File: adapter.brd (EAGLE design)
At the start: 88.6 x 82.5 mm, 11 parts

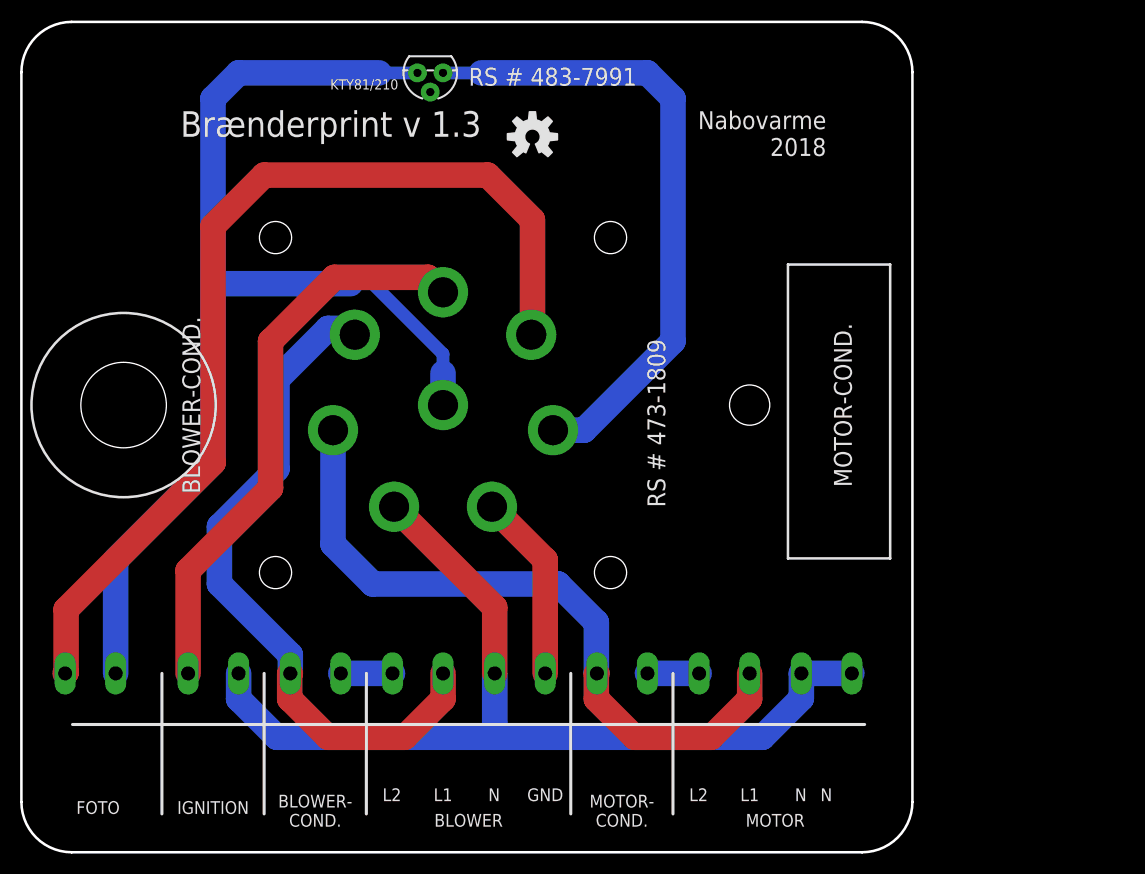
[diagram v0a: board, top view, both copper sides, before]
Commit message: new version (v.1.4)
socket pin spacing changed from 5,02 mm to 5 mm

grouped photo and ignition connectors

added more silk info

wider pcb with space for capacitor hole mount
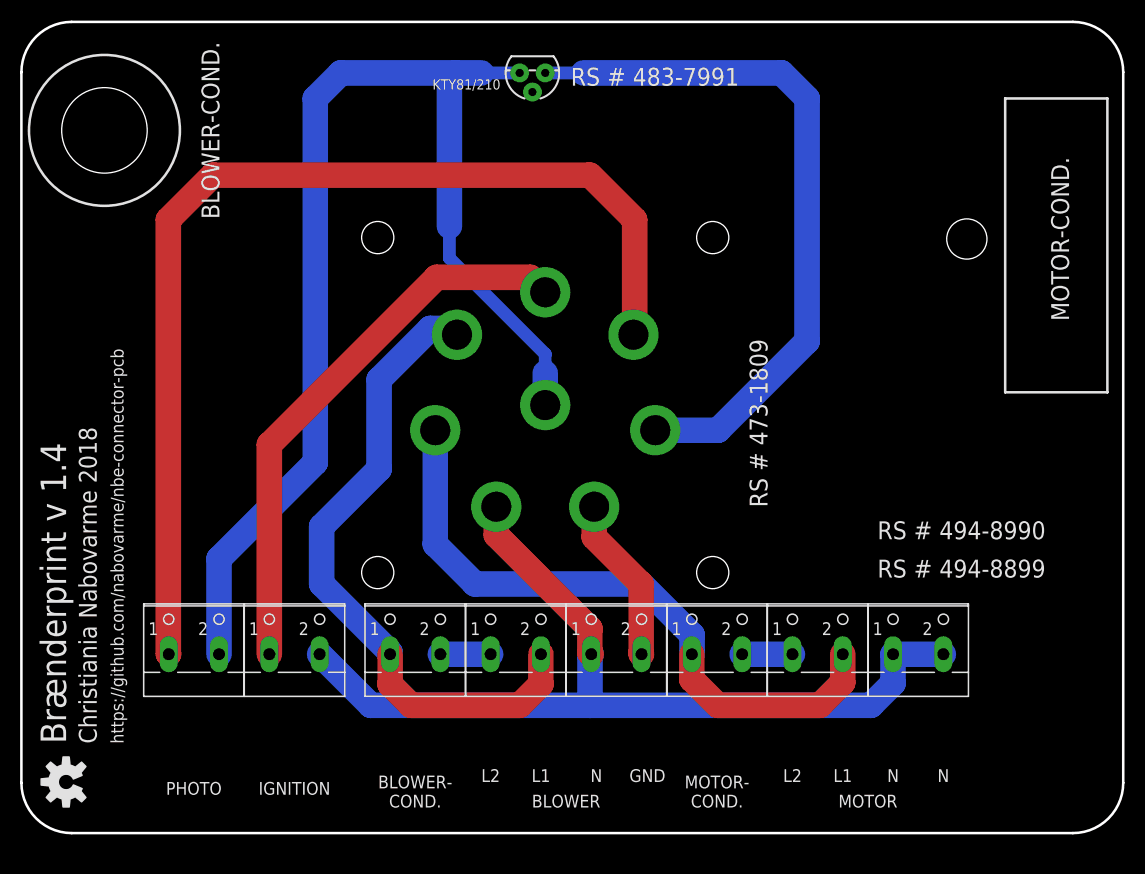
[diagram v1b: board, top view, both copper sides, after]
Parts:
- removed BLOWER1, FOTO, MOTOR1: (no value), SparkFun (old):1X02_LONGPADS
- added BLOWER-2, MOTOR-2, PHOTO: (no value), con-wago-500:W237-102
- BLOWER, BLOWER-COND., IGNITION, MOTOR, MOTOR-COND.: device SparkFun (old):1X02_LONGPADS -> con-wago-500:W237-102
- moved U$2 79.1 mm to (5.71, 4.45), turned to 90 degrees
- moved KTY81/210 10.2 mm to (52.1, 74.9)
- moved U$1 10.2 mm to (53.3, 41.9)
- moved BLOWER-COND. 8.05 mm to (40.4, 18.4), turned to 0 degrees
- moved BLOWER 7.90 mm to (50.4, 18.4), turned to 0 degrees
- moved MOTOR-COND. 7.61 mm to (70.4, 18.4), turned to 0 degrees
- moved MOTOR 7.46 mm to (80.4, 18.4), turned to 0 degrees
- moved IGNITION 6.40 mm to (28.4, 18.4), turned to 0 degrees
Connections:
- net GND: now also BLOWER-2.1, IGNITION.2, MOTOR-2.1, MOTOR-2.2; no longer BLOWER1.2, IGNITION.1, MOTOR1.1, MOTOR1.2
- net N$1: now also PHOTO.1; no longer FOTO.1
- net N$10: now also MOTOR-COND..1, MOTOR.2; no longer MOTOR-COND..2, MOTOR.1
- net N$2: now also IGNITION.1; no longer IGNITION.2
- net N$3: now also PHOTO.2; no longer FOTO.2
- net N$5: now also MOTOR-COND..2, MOTOR.1; no longer MOTOR-COND..1, MOTOR.2
- net N$7: now also BLOWER-COND..1, BLOWER.2; no longer BLOWER-COND..2, BLOWER.1
- net N$8: now also BLOWER-2.2; no longer BLOWER1.1
- net N$9: now also BLOWER-COND..2, BLOWER.1; no longer BLOWER-COND..1, BLOWER.2
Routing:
- net N$1: track 97.7 -> 104.7 mm
- net N$4: track 63.6 -> 70.0 mm
- net GND: track 96.2 -> 91.6 mm
- net N$10: track 69.3 -> 64.9 mm
- net N$3: track 113.4 -> 117.8 mm
- net N$7: track 68.1 -> 65.3 mm
- net N$8: track 18.8 -> 16.6 mm
- net N$2: track 56.8 -> 55.8 mm
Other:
- board size 88.6 x 82.5 mm -> 109.5 x 80.6 mm
- board text added: "Brænderprint v 1.4"
- board text added: "Christiania Nabovarme 2018"
- board text added: "PHOTO"
- board text added: "RS # 494-8899"
- board text added: "RS # 494-8990"
- board text added: "https://github.com/nabovarme/nbe-connector-pcb"
- board text removed: "Brænderprint v 1.3"
- board text removed: "FOTO"
- board text removed: "Nabovarme 2018"

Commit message: center aligned main connector on pcb
version 1.4.1
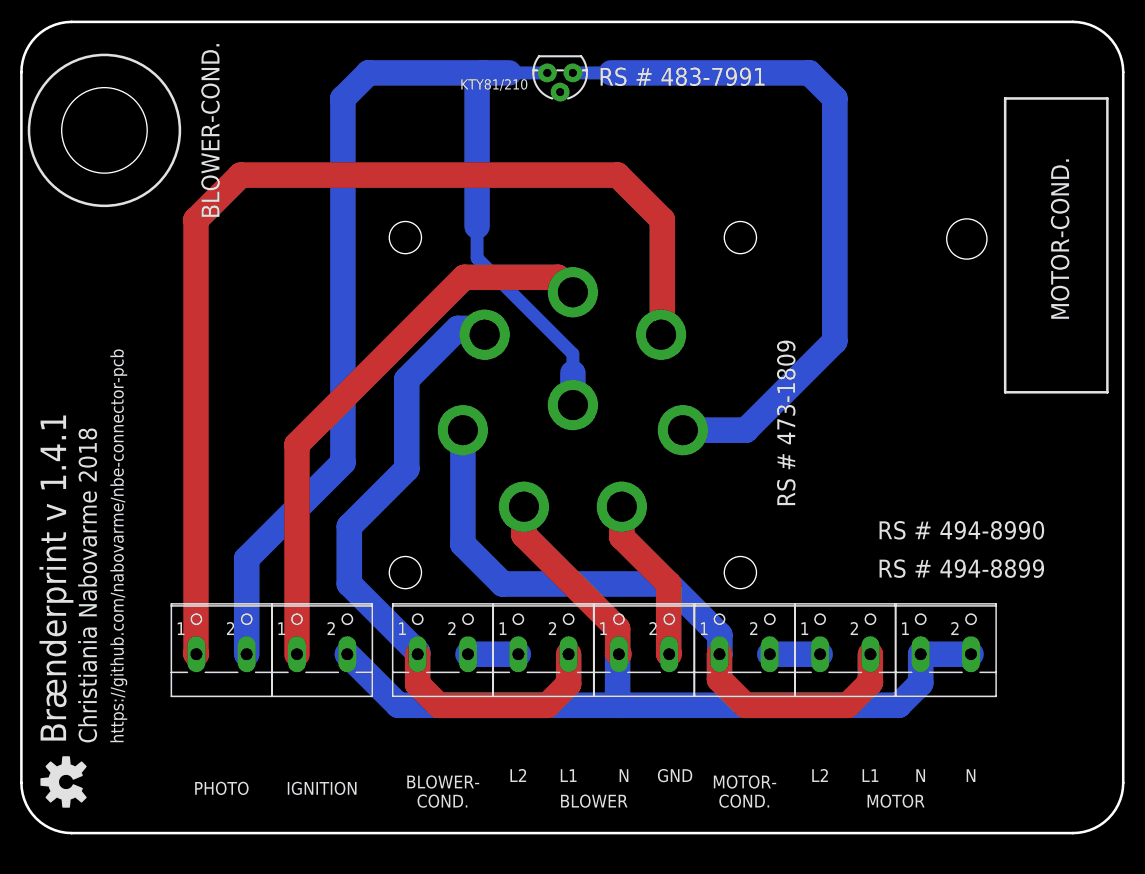
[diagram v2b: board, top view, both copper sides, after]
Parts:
- moved BLOWER 2.75 mm to (53.2, 18.4)
- moved BLOWER-2 2.75 mm to (63.2, 18.4)
- moved BLOWER-COND. 2.75 mm to (43.2, 18.4)
- moved IGNITION 2.75 mm to (31.2, 18.4)
- moved KTY81/210 2.75 mm to (54.8, 74.9)
- moved MOTOR 2.75 mm to (83.2, 18.4)
- moved MOTOR-2 2.75 mm to (93.2, 18.4)
- moved MOTOR-COND. 2.75 mm to (73.2, 18.4)
- moved PHOTO 2.75 mm to (21.2, 18.4)
- moved U$1 2.75 mm to (56.1, 41.9)
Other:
- board text added: "Brænderprint v 1.4.1"
- board text removed: "Brænderprint v 1.4"
